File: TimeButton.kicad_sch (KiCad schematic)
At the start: 32 parts, among them J1 TagConnect, J3 USB_C_Receptacle_USB2.0_16P, U1 STM32F042G4Ux, U2 NCP1117ST33T3G, U3 M24C02-FMN

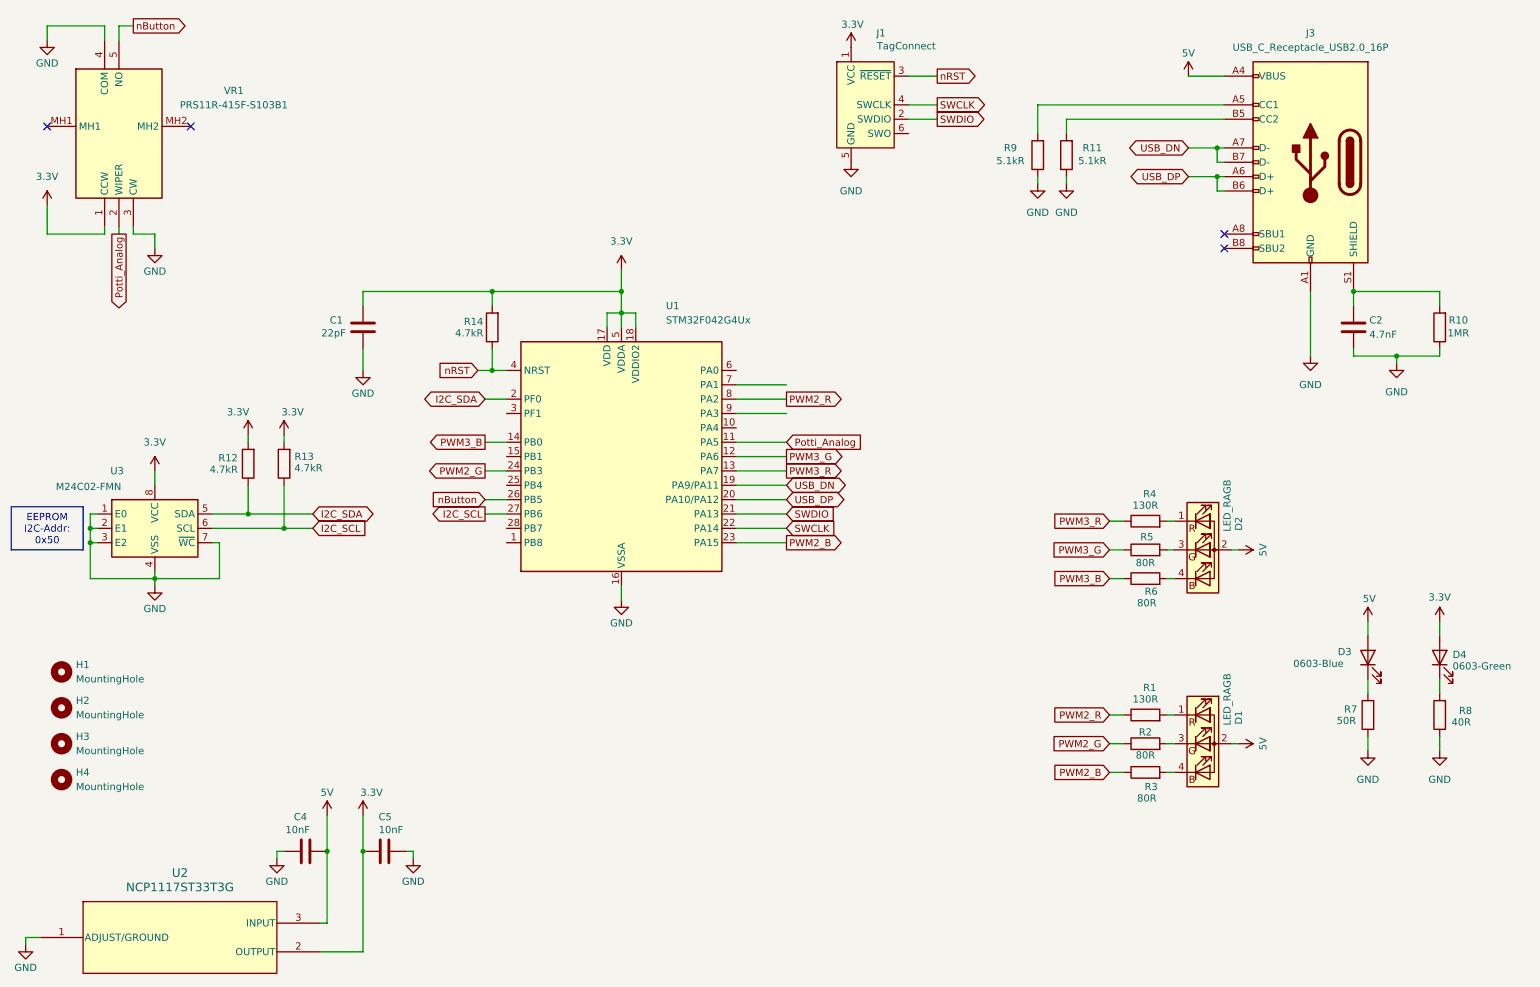
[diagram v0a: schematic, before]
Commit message: Added two GPIO Connectors for additional use
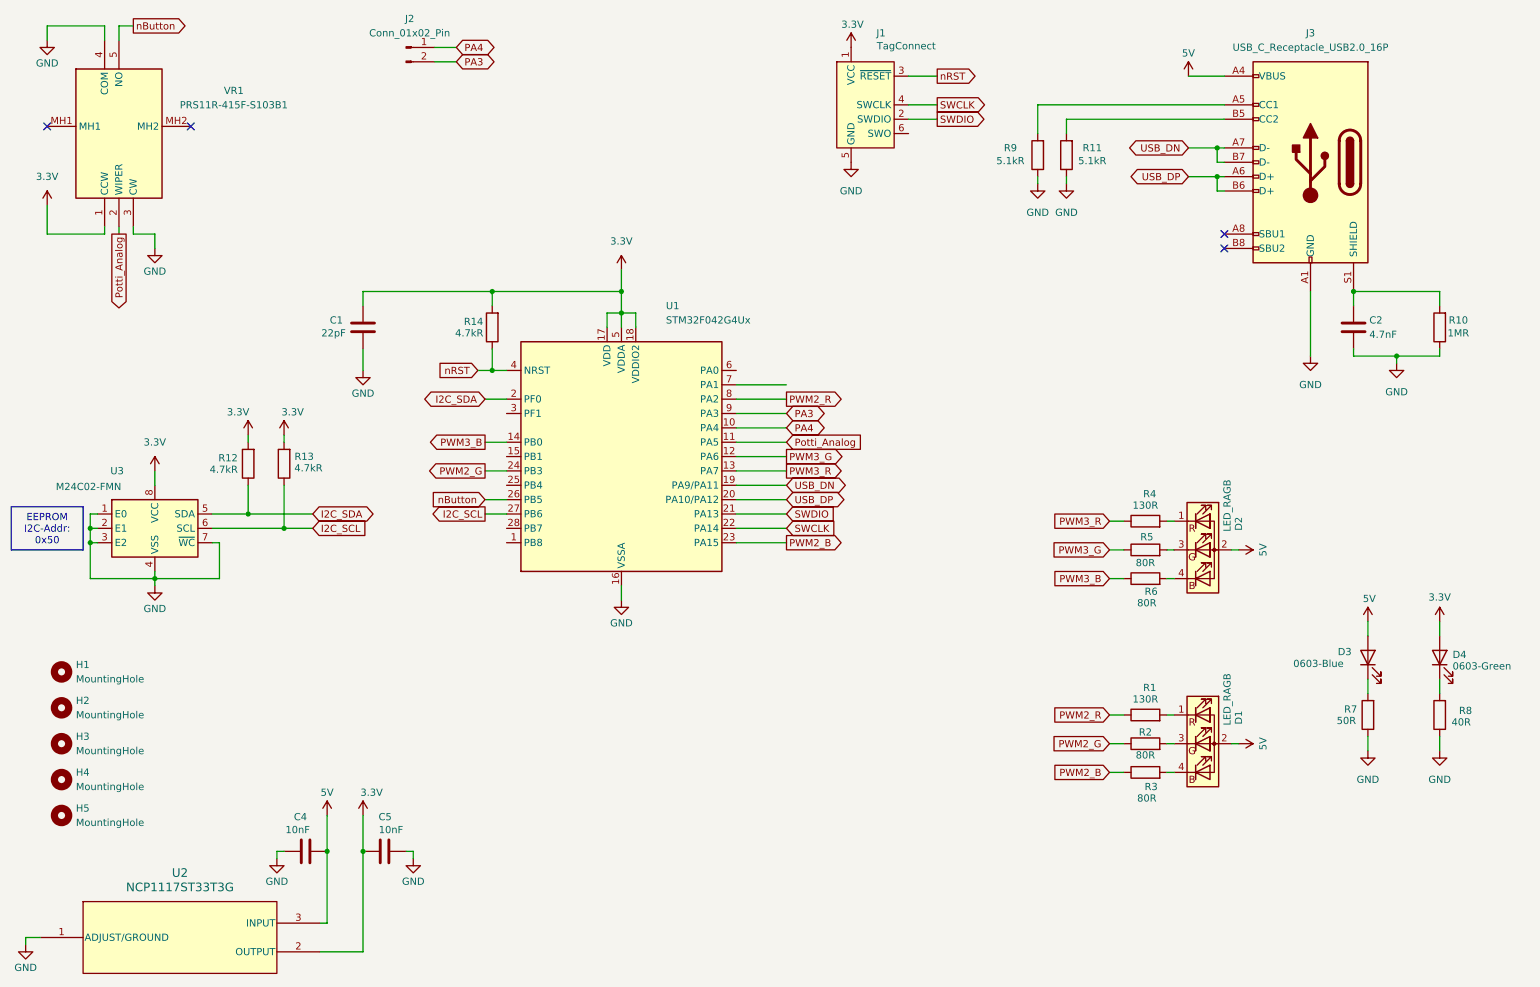
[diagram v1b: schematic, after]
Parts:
- added H5: MountingHole, MountingHole:MountingHole_2.2mm_M2_DIN965, symbol Mechanical:MountingHole
- added J2: Conn_01x02_Pin, Connector_PinHeader_2.54mm:PinHeader_1x02_P2.54mm_Vertical, symbol Connector:Conn_01x02_Pin
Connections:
- net PA4: now reaches U1.10 (PA4)
- net PA4: now also J2.1 (Pin_1)
- net PA3: now reaches U1.9 (PA3)
- net PA3: now also J2.2 (Pin_2)
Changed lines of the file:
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@@
 	(wire
 		(pts
+			(xy 90.17 27.94) (xy 93.98 27.94)
+		)
+		(stroke
+			(width 0)
+			(type default)
+		)
+	)
+	(wire
+		(pts
 			(xy 40.64 118.11) (xy 40.64 119.38)
 		)
@@
 	(wire
 		(pts
+			(xy 90.17 25.4) (xy 93.98 25.4)
+		)
+		(stroke
+			(width 0)
+			(type default)
+		)
+	)
+	(wire
+		(pts
 			(xy 123.19 120.65) (xy 123.19 123.19)
 		)
@@
 	(wire
 		(pts
+			(xy 143.51 92.71) (xy 152.4 92.71)
+		)
+		(stroke
+			(width 0)
+			(type default)
+		)
+	)
+	(wire
+		(pts
 			(xy 229.87 50.8) (xy 228.6 50.8)
 		)
@@
 		)
 	)
+	(global_label "PA4"
+		(shape bidirectional)
+		(at 93.98 25.4 0)
+		(fields_autoplaced yes)
+		(effects
+			(font
+				(size 1.27 1.27)
+			)
+			(justify left)
+		)
+		(property "Intersheetrefs" "${INTERSHEET_REFS}"
+			(at 100.5333 25.4 0)
+			(effects
+				(font
+					(size 1.27 1.27)
+				)
+				(justify left)
+				(hide yes)
+			)
+		)
+	)
 	(global_label "PWM2_R"
 		(shape output)
@@
 		)
 	)
+	(global_label "PA3"
+		(shape bidirectional)
+		(at 152.4 90.17 0)
+		(fields_autoplaced yes)
+		(effects
+			(font
+				(size 1.27 1.27)
+			)
+			(justify left)
+		)
+		(property "Intersheetrefs" "${INTERSHEET_REFS}"
+			(at 158.9533 90.17 0)
+			(effects
+				(font
+					(size 1.27 1.27)
+				)
+				(justify left)
+				(hide yes)
+			)
+		)
+	)
 	(global_label "Potti_Analog"
 		(shape input)
@@
 		)
 	)
+	(global_label "PA4"
+		(shape bidirectional)
+		(at 152.4 92.71 0)
+		(fields_autoplaced yes)
+		(effects
+			(font
+				(size 1.27 1.27)
+			)
+			(justify left)
+		)
+		(property "Intersheetrefs" "${INTERSHEET_REFS}"
+			(at 158.9533 92.71 0)
+			(effects
+				(font
+					(size 1.27 1.27)
+				)
+				(justify left)
+				(hide yes)
+			)
+		)
+	)
 	(global_label "PWM2_B"
 		(shape output)
@@
 		)
 	)
+	(global_label "PA3"
+		(shape bidirectional)
+		(at 93.98 27.94 0)
+		(fields_autoplaced yes)
+		(effects
+			(font
+				(size 1.27 1.27)
+			)
+			(justify left)
+		)
+		(property "Intersheetrefs" "${INTERSHEET_REFS}"
+			(at 100.5333 27.94 0)
+			(effects
+				(font
+					(size 1.27 1.27)
+				)
+				(justify left)
+				(hide yes)
+			)
+		)
+	)
 	(global_label "PWM3_G"
 		(shape output)
@@
 	)
 	(symbol
+		(lib_id "Connector:Conn_01x02_Pin")
+		(at 85.09 25.4 0)
+		(unit 1)
+		(exclude_from_sim no)
+		(in_bom yes)
+		(on_board yes)
+		(dnp no)
+		(fields_autoplaced yes)
+		(property "Reference" "J2"
+			(at 85.725 20.32 0)
+			(effects
+				(font
+					(size 1.27 1.27)
+				)
+			)
+		)
+		(property "Value" "Conn_01x02_Pin"
+			(at 85.725 22.86 0)
+			(effects
+				(font
+					(size 1.27 1.27)
+				)
+			)
+		)
+		(property "Footprint" "Connector_PinHeader_2.54mm:PinHeader_1x02_P2.54mm_Vertical"
+			(at 85.09 25.4 0)
+			(effects
+				(font
+					(size 1.27 1.27)
+				)
+				(hide yes)
+			)
+		)
+		(property "Datasheet" "~"
+			(at 85.09 25.4 0)
+			(effects
+				(font
+					(size 1.27 1.27)
+				)
+				(hide yes)
+			)
+		)
+		(property "Description" "Generic connector, single row, 01x02, script generated"
+			(at 85.09 25.4 0)
+			(effects
+				(font
+					(size 1.27 1.27)
+				)
+				(hide yes)
+			)
+		)
+		(pin "2"
+		)
+		(pin "1"
+		)
+		(instances
+			(project ""
+				(path "/b8d0d559-03bf-427f-9068-e35467cdde18"
+					(reference "J2")
+					(unit 1)
+				)
+			)
+		)
+	)
+	(symbol
 		(lib_id "power:+3.3V")
 		(at 21.59 53.34 0)
@@
 					(unit 1)
 				)
+			)
+		)
+	)
+	(symbol
+		(lib_id "Mechanical:MountingHole")
+		(at 24.13 161.29 0)
+		(unit 1)
+		(exclude_from_sim yes)
+		(in_bom no)
+		(on_board yes)
+		(dnp no)
+		(fields_autoplaced yes)
+		(property "Reference" "H5"
+			(at 26.67 160.0199 0)
+			(effects
+				(font
+					(size 1.27 1.27)
+				)
+				(justify left)
+			)
+		)
+		(property "Value" "MountingHole"
+			(at 26.67 162.5599 0)
+			(effects
+				(font
+					(size 1.27 1.27)
+				)
+				(justify left)
+			)
+		)
+		(property "Footprint" "MountingHole:MountingHole_2.2mm_M2_DIN965"
+			(at 24.13 161.29 0)
+			(effects
+				(font
+					(size 1.27 1.27)
+				)
+				(hide yes)
+			)
+		)
+		(property "Datasheet" "~"
+			(at 24.13 161.29 0)
+			(effects
+				(font
+					(size 1.27 1.27)
+				)
+				(hide yes)
+			)
+		)
+		(property "Description" "Mounting Hole without connection"
+			(at 24.13 161.29 0)
+			(effects
+				(font
+					(size 1.27 1.27)
+				)
+				(hide yes)
+			)
+		)
+		(instances
+			(project "TimeButton"
+				(path "/b8d0d559-03bf-427f-9068-e35467cdde18"
+					(reference "H5")
+					(unit 1)
+				)

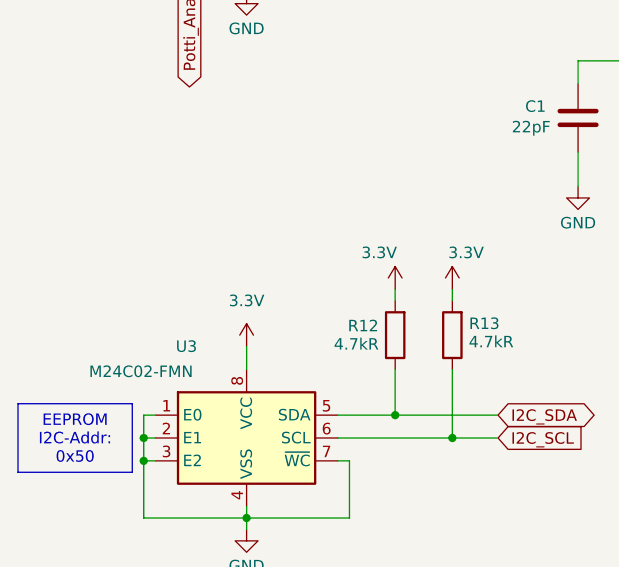
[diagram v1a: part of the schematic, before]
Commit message: Added Capacitor for EEPROM
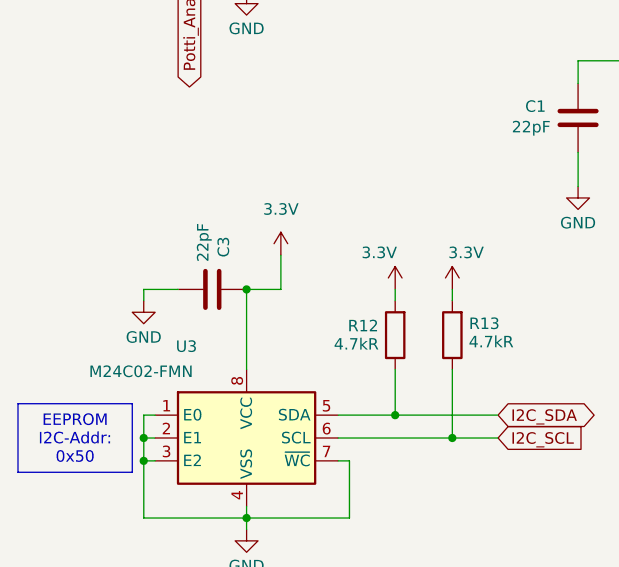
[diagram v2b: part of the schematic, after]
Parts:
- added C3: 22pF, Capacitor_SMD:C_0805_2012Metric, symbol Device:C
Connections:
- net 3.3V: now also C3.2
- net GND: now also C3.1
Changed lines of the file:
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@@
 	)
 	(junction
+		(at 40.64 93.98)
+		(diameter 0)
+		(color 0 0 0 0)
+	)
+	(junction
 		(at 63.5 110.49)
 		(diameter 0)
@@
 	(wire
 		(pts
+			(xy 29.21 95.25) (xy 29.21 93.98)
+		)
+		(stroke
+			(width 0)
+			(type default)
+		)
+	)
+	(wire
+		(pts
 			(xy 29.21 110.49) (xy 29.21 113.03)
 		)
@@
 	(wire
 		(pts
+			(xy 44.45 90.17) (xy 44.45 93.98)
+		)
+		(stroke
+			(width 0)
+			(type default)
+		)
+	)
+	(wire
+		(pts
 			(xy 143.51 105.41) (xy 152.4 105.41)
 		)
@@
 	(wire
 		(pts
+			(xy 44.45 93.98) (xy 40.64 93.98)
+		)
+		(stroke
+			(width 0)
+			(type default)
+		)
+	)
+	(wire
+		(pts
 			(xy 123.19 120.65) (xy 123.19 123.19)
 		)
@@
 	(wire
 		(pts
-			(xy 77.47 167.64) (xy 77.47 185.42)
+			(xy 29.21 93.98) (xy 33.02 93.98)
 		)
 		(stroke
@@
 	(wire
 		(pts
-			(xy 228.6 48.26) (xy 229.87 48.26)
+			(xy 77.47 167.64) (xy 77.47 185.42)
 		)
 		(stroke
@@
 	(wire
 		(pts
-			(xy 220.98 114.3) (xy 219.71 114.3)
+			(xy 228.6 48.26) (xy 229.87 48.26)
 		)
 		(stroke
@@
 	(wire
 		(pts
-			(xy 245.11 68.58) (xy 245.11 80.01)
+			(xy 220.98 114.3) (xy 219.71 114.3)
 		)
 		(stroke
@@
 	(wire
 		(pts
-			(xy 40.64 100.33) (xy 40.64 102.87)
+			(xy 245.11 68.58) (xy 245.11 80.01)
 		)
 		(stroke
@@
 	(wire
 		(pts
+			(xy 40.64 93.98) (xy 40.64 102.87)
+		)
+		(stroke
+			(width 0)
+			(type default)
+		)
+	)
+	(wire
+		(pts
 			(xy 52.07 113.03) (xy 50.8 113.03)
 		)
@@
 	(symbol
 		(lib_id "power:+3.3V")
-		(at 40.64 100.33 0)
+		(at 44.45 90.17 0)
 		(unit 1)
 		(exclude_from_sim no)
@@
 		(fields_autoplaced yes)
 		(property "Reference" "#PWR017"
-			(at 40.64 104.14 0)
+			(at 44.45 93.98 0)
 			(effects
 				(font
@@
 		)
 		(property "Value" "3.3V"
-			(at 40.64 95.25 0)
+			(at 44.45 85.09 0)
 			(effects
 				(font
@@
 		)
 		(property "Footprint" ""
-			(at 40.64 100.33 0)
+			(at 44.45 90.17 0)
 			(effects
 				(font
@@
 		)
 		(property "Datasheet" ""
-			(at 40.64 100.33 0)
+			(at 44.45 90.17 0)
 			(effects
 				(font
@@
 		)
 		(property "Description" "Power symbol creates a global label with name \"+3.3V\""
-			(at 40.64 100.33 0)
+			(at 44.45 90.17 0)
 			(effects
 				(font
@@
 	)
 	(symbol
+		(lib_id "Device:C")
+		(at 36.83 93.98 90)
+		(unit 1)
+		(exclude_from_sim no)
+		(in_bom yes)
+		(on_board yes)
+		(dnp no)
+		(property "Reference" "C3"
+			(at 38.1 90.424 0)
+			(effects
+				(font
+					(size 1.27 1.27)
+				)
+				(justify left)
+			)
+		)
+		(property "Value" "22pF"
+			(at 35.814 90.932 0)
+			(effects
+				(font
+					(size 1.27 1.27)
+				)
+				(justify left)
+			)
+		)
+		(property "Footprint" "Capacitor_SMD:C_0805_2012Metric"
+			(at 40.64 93.0148 0)
+			(effects
+				(font
+					(size 1.27 1.27)
+				)
+				(hide yes)
+			)
+		)
+		(property "Datasheet" "~"
+			(at 36.83 93.98 0)
+			(effects
+				(font
+					(size 1.27 1.27)
+				)
+				(hide yes)
+			)
+		)
+		(property "Description" "Unpolarized capacitor"
+			(at 36.83 93.98 0)
+			(effects
+				(font
+					(size 1.27 1.27)
+				)
+				(hide yes)
+			)
+		)
+		(pin "2"
+		)
+		(pin "1"
+		)
+		(instances
+			(project "TimeButton"
+				(path "/b8d0d559-03bf-427f-9068-e35467cdde18"
+					(reference "C3")
+					(unit 1)
+				)
+			)
+		)
+	)
+	(symbol
 		(lib_id "power:GND")
 		(at 86.36 168.91 0)
@@
 					(unit 1)
 				)
+			)
+		)
+	)
+	(symbol
+		(lib_id "power:GND")
+		(at 29.21 95.25 0)
+		(unit 1)
+		(exclude_from_sim no)
+		(in_bom yes)
+		(on_board yes)
+		(dnp no)
+		(property "Reference" "#PWR021"
+			(at 29.21 101.6 0)
+			(effects
+				(font
+					(size 1.27 1.27)
+				)
+				(hide yes)
+			)
+		)
+		(property "Value" "GND"
+			(at 29.21 99.314 0)
+			(effects
+				(font
+					(size 1.27 1.27)
+				)
+			)
+		)
+		(property "Footprint" ""
+			(at 29.21 95.25 0)
+			(effects
+				(font
+					(size 1.27 1.27)
+				)
+				(hide yes)
+			)
+		)
+		(property "Datasheet" ""
+			(at 29.21 95.25 0)
+			(effects
+				(font
+					(size 1.27 1.27)
+				)
+				(hide yes)
+			)
+		)
+		(property "Description" "Power symbol creates a global label with name \"GND\" , ground"
+			(at 29.21 95.25 0)
+			(effects
+				(font
+					(size 1.27 1.27)
+				)
+				(hide yes)
+			)
+		)
+		(pin "1"
+		)
+		(instances
+			(project "TimeButton"
+				(path "/b8d0d559-03bf-427f-9068-e35467cdde18"
+					(reference "#PWR021")
+					(unit 1)
+				)
